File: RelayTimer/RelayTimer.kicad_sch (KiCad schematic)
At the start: 20 parts, among them J1 Jack-DC, J2 Relay_Con, Q1 2N3904, U1 ATtiny85-20P

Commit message: minor update to KiCad project
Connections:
- net +5V: now also R6.1; no longer R6.2
- net PB3_PULLUP: now also R6.2; no longer R6.1
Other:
- moved on the sheet: R6

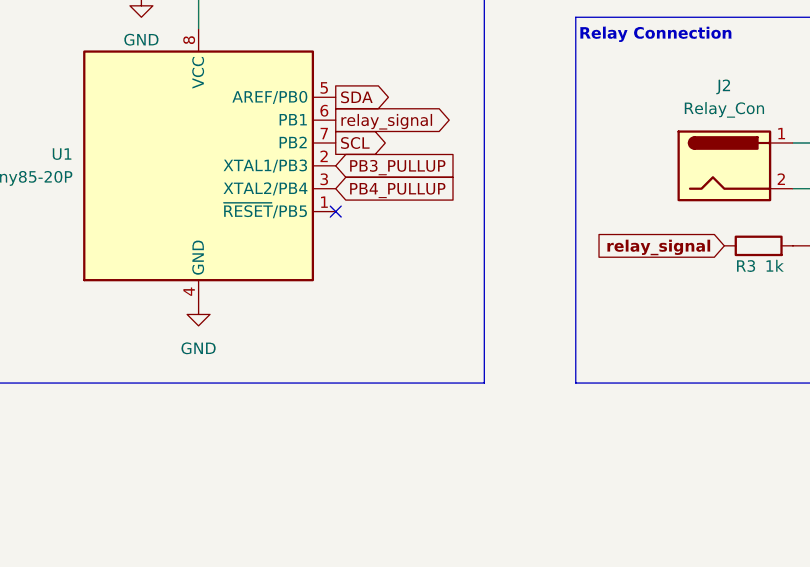
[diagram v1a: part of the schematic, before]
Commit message: added small reset button to schematic
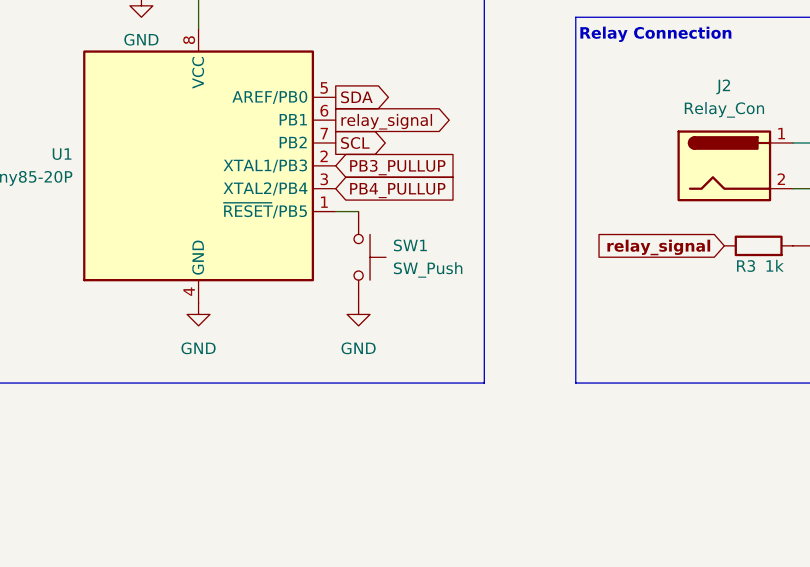
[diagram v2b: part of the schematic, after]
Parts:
- added SW1: SW_Push, Button_Switch_THT:SW_PUSH_6mm, symbol Switch:SW_Push
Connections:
- net GND: now also SW1.2
- net at U1.1 (~{RESET}/PB5): now also SW1.1
- no-connect marks 1 -> 0
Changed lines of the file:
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@@
 		(color 0 0 0 0)
 	)
-	(no_connect
-		(at 162.56 116.84)
-	)
 	(wire
 		(pts
@@
 	(wire
 		(pts
+			(xy 162.56 116.84) (xy 165.1 116.84)
+		)
+		(stroke
+			(width 0)
+			(type default)
+		)
+	)
+	(wire
+		(pts
 			(xy 55.88 77.47) (xy 55.88 80.01)
 		)
@@
 	)
 	(symbol
+		(lib_id "power:GND")
+		(at 165.1 127 0)
+		(unit 1)
+		(exclude_from_sim no)
+		(in_bom yes)
+		(on_board yes)
+		(dnp no)
+		(fields_autoplaced yes)
+		(property "Reference" "#PWR014"
+			(at 165.1 133.35 0)
+			(effects
+				(font
+					(size 1.27 1.27)
+				)
+				(hide yes)
+			)
+		)
+		(property "Value" "GND"
+			(at 165.1 132.08 0)
+			(effects
+				(font
+					(size 1.27 1.27)
+				)
+			)
+		)
+		(property "Footprint" ""
+			(at 165.1 127 0)
+			(effects
+				(font
+					(size 1.27 1.27)
+				)
+				(hide yes)
+			)
+		)
+		(property "Datasheet" ""
+			(at 165.1 127 0)
+			(effects
+				(font
+					(size 1.27 1.27)
+				)
+				(hide yes)
+			)
+		)
+		(property "Description" "Power symbol creates a global label with name \"GND\" , ground"
+			(at 165.1 127 0)
+			(effects
+				(font
+					(size 1.27 1.27)
+				)
+				(hide yes)
+			)
+		)
+		(pin "1"
+		)
+		(instances
+			(project ""
+				(path "/c516751d-6636-4ecf-81a9-f6291dd07648"
+					(reference "#PWR014")
+					(unit 1)
+				)
+			)
+		)
+	)
+	(symbol
 		(lib_id "power:+5V")
 		(at 96.52 119.38 0)
@@
 					(unit 1)
 				)
+			)
+		)
+	)
+	(symbol
+		(lib_id "Switch:SW_Push")
+		(at 165.1 121.92 270)
+		(unit 1)
+		(exclude_from_sim no)
+		(in_bom yes)
+		(on_board yes)
+		(dnp no)
+		(fields_autoplaced yes)
+		(property "Reference" "SW1"
+			(at 168.91 120.6499 90)
+			(effects
+				(font
+					(size 1.27 1.27)
+				)
+				(justify left)
+			)
+		)
+		(property "Value" "SW_Push"
+			(at 168.91 123.1899 90)
+			(effects
+				(font
+					(size 1.27 1.27)
+				)
+				(justify left)
+			)
+		)
+		(property "Footprint" "Button_Switch_THT:SW_PUSH_6mm"
+			(at 170.18 121.92 0)
+			(effects
+				(font
+					(size 1.27 1.27)
+				)
+				(hide yes)
+			)
+		)
+		(property "Datasheet" "~"
+			(at 170.18 121.92 0)
+			(effects
+				(font
+					(size 1.27 1.27)
+				)
+				(hide yes)
+			)
+		)
+		(property "Description" "Push button switch, generic, two pins"
+			(at 165.1 121.92 0)
+			(effects
+				(font
+					(size 1.27 1.27)
+				)
+				(hide yes)
+			)
+		)
+		(pin "1"
+		)
+		(pin "2"
+		)
+		(instances
+			(project ""
+				(path "/c516751d-6636-4ecf-81a9-f6291dd07648"
+					(reference "SW1")
+					(unit 1)
+				)

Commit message: fixed small issue and updated board
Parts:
- removed R4, R5: 1k, Resistor_THT:R_Axial_DIN0204_L3.6mm_D1.6mm_P2.54mm_Vertical, symbol Device:R
- R6, R7: footprint Resistor_THT:R_Axial_DIN0204_L3.6mm_D1.6mm_P2.54mm_Vertical -> Resistor_THT:R_Axial_DIN0204_L3.6mm_D1.6mm_P7.62mm_Horizontal
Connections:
- net +5V: now also R6.2, R7.2; no longer R6.1, R7.1
- net PB3_PULLUP: now also R6.1, START/STOP1.2; no longer R6.2
- net PB4_PULLUP: now also FUNCTION1.2, R7.1; no longer R7.2
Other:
- moved on the sheet: C3, C4, R6, R7
